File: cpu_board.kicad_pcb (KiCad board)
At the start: 2 copper layers, 19 parts, among them P1 USB_B, SW1 SW_PUSH, U1 MC6809, U2 MC6850, U3 NE555, U4 74HC04, Y1 4MHz

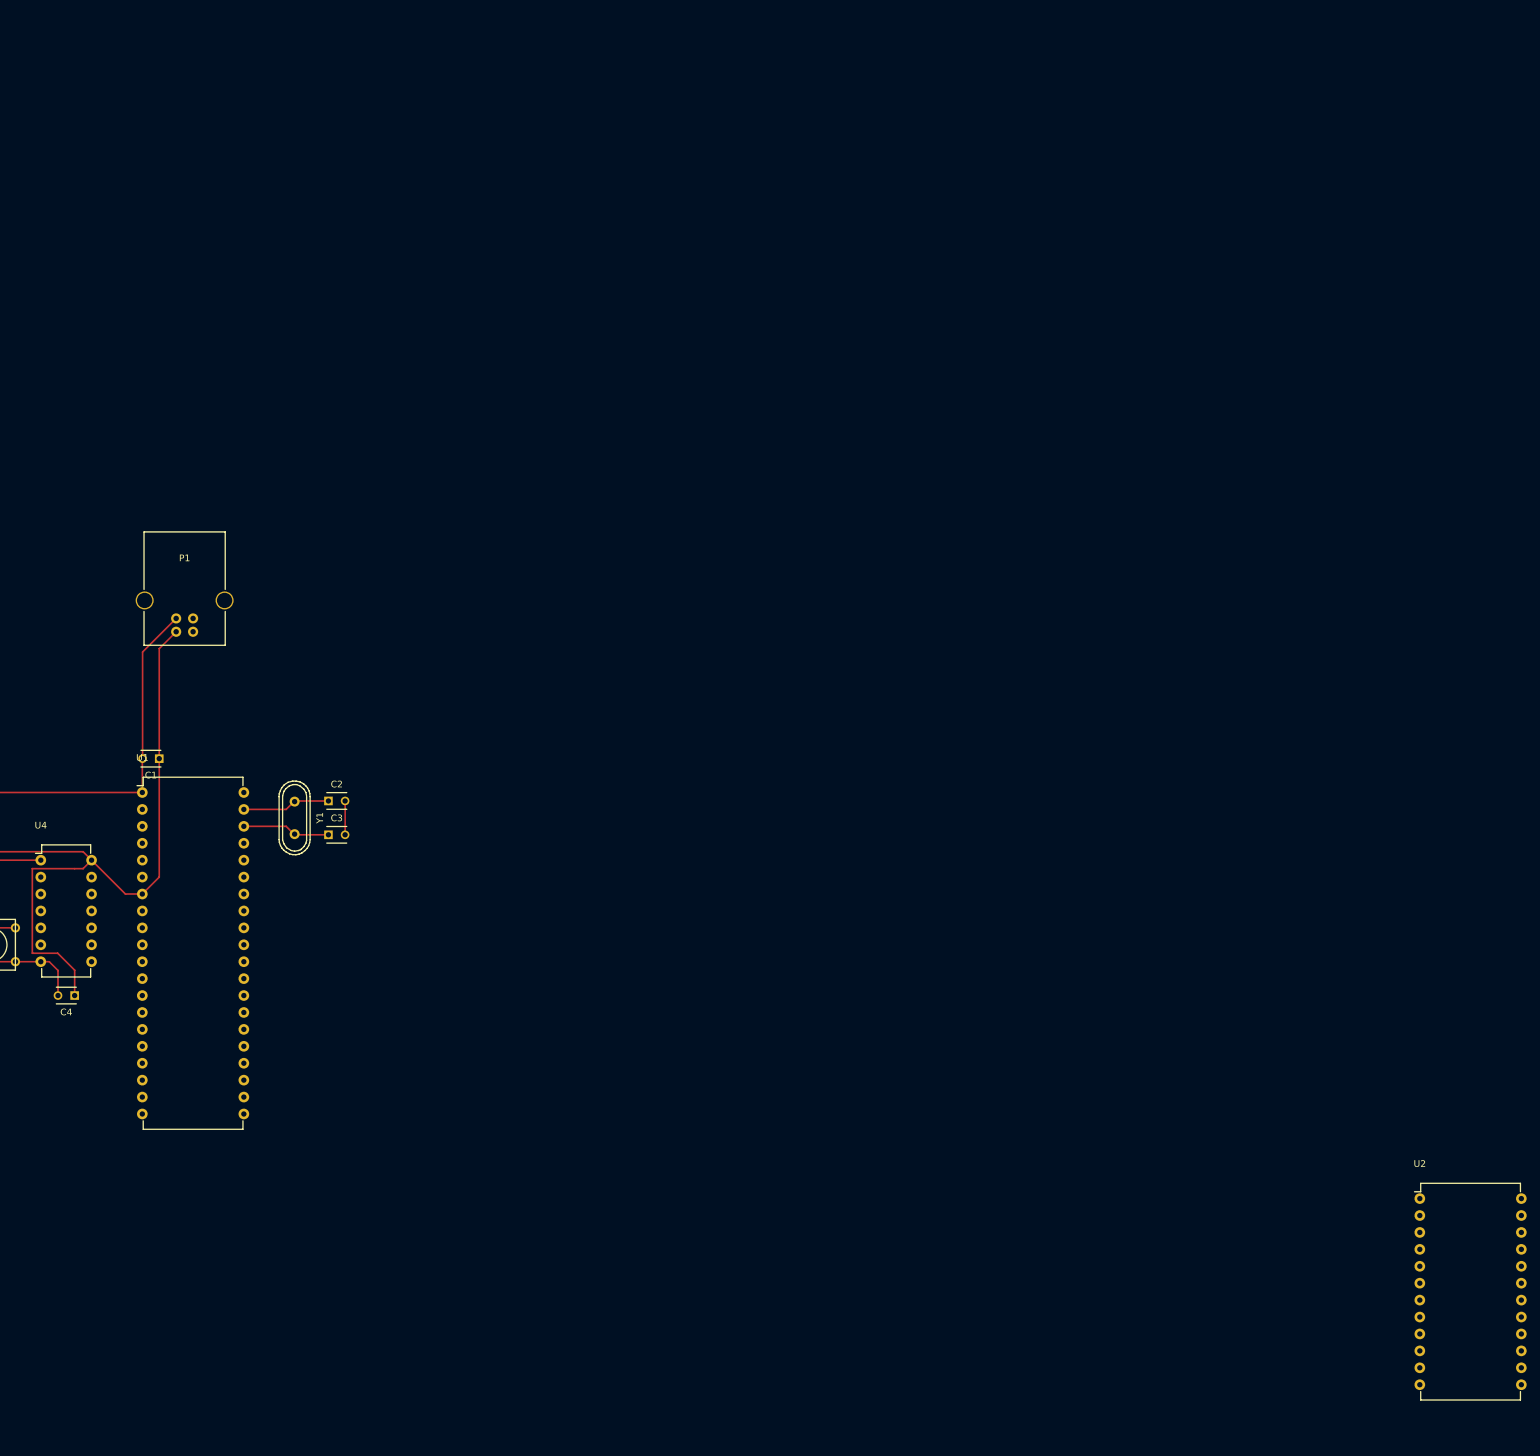
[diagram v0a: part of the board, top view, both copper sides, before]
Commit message: Added initial banking schematics
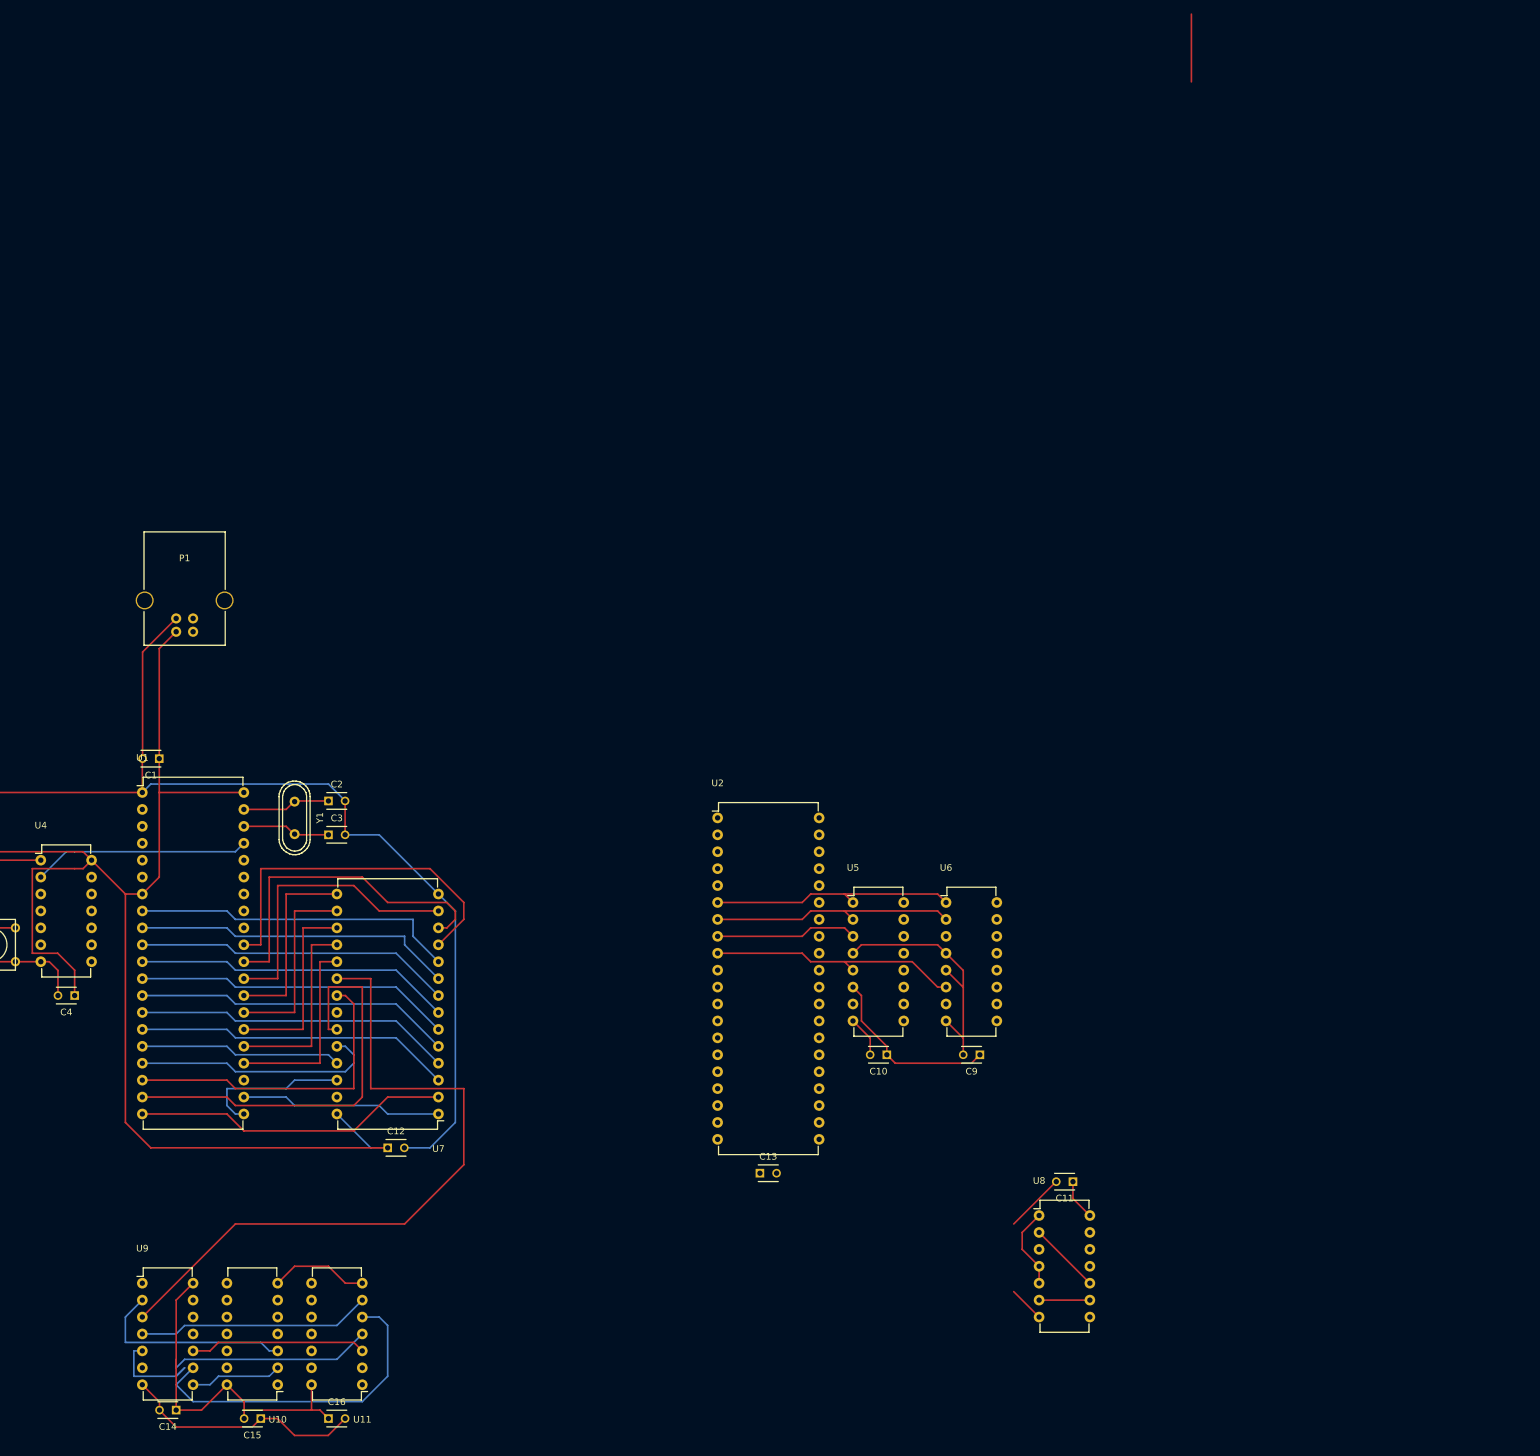
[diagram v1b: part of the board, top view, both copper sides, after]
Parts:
- added C10: 100nF, Capacitors_ThroughHole:C_Disc_D3_P2.5, F.Cu at (185.4, 118.1)
- added C11: 100nF, Capacitors_ThroughHole:C_Disc_D3_P2.5, F.Cu at (213.4, 137.2)
- added C12: 100nF, Capacitors_ThroughHole:C_Disc_D3_P2.5, F.Cu at (110.5, 132.1)
- added C13: 100nF, Capacitors_ThroughHole:C_Disc_D3_P2.5, F.Cu at (166.4, 135.9)
- added C14: 100nF, Capacitors_ThroughHole:C_Disc_D3_P2.5, F.Cu at (78.7, 171.4)
- added C15: 100nF, Capacitors_ThroughHole:C_Disc_D3_P2.5, F.Cu at (91.4, 172.7)
- added C16: 100nF, Capacitors_ThroughHole:C_Disc_D3_P2.5, F.Cu at (101.6, 172.7)
- added C9: 100nF, Capacitors_ThroughHole:C_Disc_D3_P2.5, F.Cu at (199.4, 118.1)
- added U10: 7400, Housings_DIP:DIP-14_W7.62mm, F.Cu at (94.0, 167.6)
- added U11: 74LS04, Housings_DIP:DIP-14_W7.62mm, F.Cu at (106.7, 167.6)
- added U5: 74LS138, Housings_DIP:DIP-16_W7.62mm, F.Cu at (180.3, 95.2)
- added U6: 74LS138, Housings_DIP:DIP-16_W7.62mm, F.Cu at (194.3, 95.2)
- added U7: HM62256BLP-7, Housings_DIP:DIP-28_W15.24mm, F.Cu at (118.1, 127.0)
- added U8: 7400, Housings_DIP:DIP-14_W7.62mm, F.Cu at (208.3, 142.2)
- added U9: 74LS08, Housings_DIP:DIP-14_W7.62mm, F.Cu at (73.7, 152.4)
- C2, C3: value 24pF -> 24/20/18/15pF
- U2: value MC6850 -> 6821; footprint Housings_DIP:DIP-24_W15.24mm -> Housings_DIP:DIP-40_W15.24mm
- Y1: value 4MHz -> 4/6/8/12MHz
- moved U2 119.9 mm to (160.0, 82.5)
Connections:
- U1 pad 10: Net-(U1-Pad10) -> A2
- U1 pad 11: Net-(U1-Pad11) -> A3
- U1 pad 12: Net-(U1-Pad12) -> A4
- U1 pad 13: Net-(U1-Pad13) -> A5
- U1 pad 14: Net-(U1-Pad14) -> A6
- U1 pad 15: Net-(U1-Pad15) -> A7
- U1 pad 16: Net-(U1-Pad16) -> A8
- U1 pad 17: Net-(U1-Pad17) -> A9
- U1 pad 18: Net-(U1-Pad18) -> A10
- U1 pad 19: Net-(U1-Pad19) -> A11
- U1 pad 20: Net-(U1-Pad20) -> A12
- U1 pad 21: Net-(U1-Pad21) -> A13
- U1 pad 22: Net-(U1-Pad22) -> A14
- U1 pad 23: Net-(U1-Pad23) -> A15
- U1 pad 24: Net-(U1-Pad24) -> D7
- U1 pad 25: Net-(U1-Pad25) -> D6
- U1 pad 26: Net-(U1-Pad26) -> D5
- U1 pad 27: Net-(U1-Pad27) -> D4
- U1 pad 28: Net-(U1-Pad28) -> D3
- U1 pad 29: Net-(U1-Pad29) -> D2
- U1 pad 30: Net-(U1-Pad30) -> D1
- U1 pad 31: Net-(U1-Pad31) -> D0
- U1 pad 32: Net-(U1-Pad32) -> /memory/R/~W~
- U1 pad 34: Net-(U1-Pad34) -> /memory/E
- U1 pad 40: Net-(U1-Pad40) -> +5V
- U1 pad 8: Net-(U1-Pad8) -> A0
- U1 pad 9: Net-(U1-Pad9) -> A1
- U2 pad 1: Net-(U2-Pad1) -> GND
- U2 pad 10: Net-(U1-Pad22) -> Net-(U2-Pad10)
- U2 pad 11: Net-(U1-Pad8) -> Net-(U2-Pad11)
- U2 pad 13: Net-(U1-Pad32) -> Net-(U2-Pad13)
- U2 pad 14: Net-(U1-Pad34) -> Net-(U2-Pad14)
- U2 pad 2: Net-(U2-Pad2) -> /memory/fixed_memory/bank
- U2 pad 20: Net-(U2-Pad20) -> +5V
- U2 pad 21: Net-(U2-Pad21) -> /memory/R/~W~
- U2 pad 3: Net-(U1-Pad34) -> Net-(U2-Pad3)
- U2 pad 4: Net-(U1-Pad34) -> Net-(U2-Pad4)
- U2 pad 8: Net-(U1-Pad23) -> Net-(U2-Pad8)
- U2 pad 9: Net-(U1-Pad21) -> Net-(U2-Pad9)
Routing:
- net GND: track 137.7 -> 342.5 mm
- net +5V: track 148.2 -> 331.7 mm
- net Net-(U7-Pad20): track 0.00 -> 104.7 mm
- net A14: track 0.00 -> 80.2 mm
- net A11: track 0.00 -> 63.3 mm
- net D0: track 0.00 -> 54.5 mm
- net D1: track 0.00 -> 50.9 mm
- net A0: track 0.00 -> 49.1 mm
- net Net-(U11-Pad4): track 0.00 -> 48.9 mm
- net A1: track 0.00 -> 48.4 mm
- net A10: track 0.00 -> 48.0 mm
- net A7: track 0.00 -> 47.6 mm
- net A5: track 0.00 -> 47.6 mm
- net A3: track 0.00 -> 47.6 mm
- net A2: track 0.00 -> 47.6 mm
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
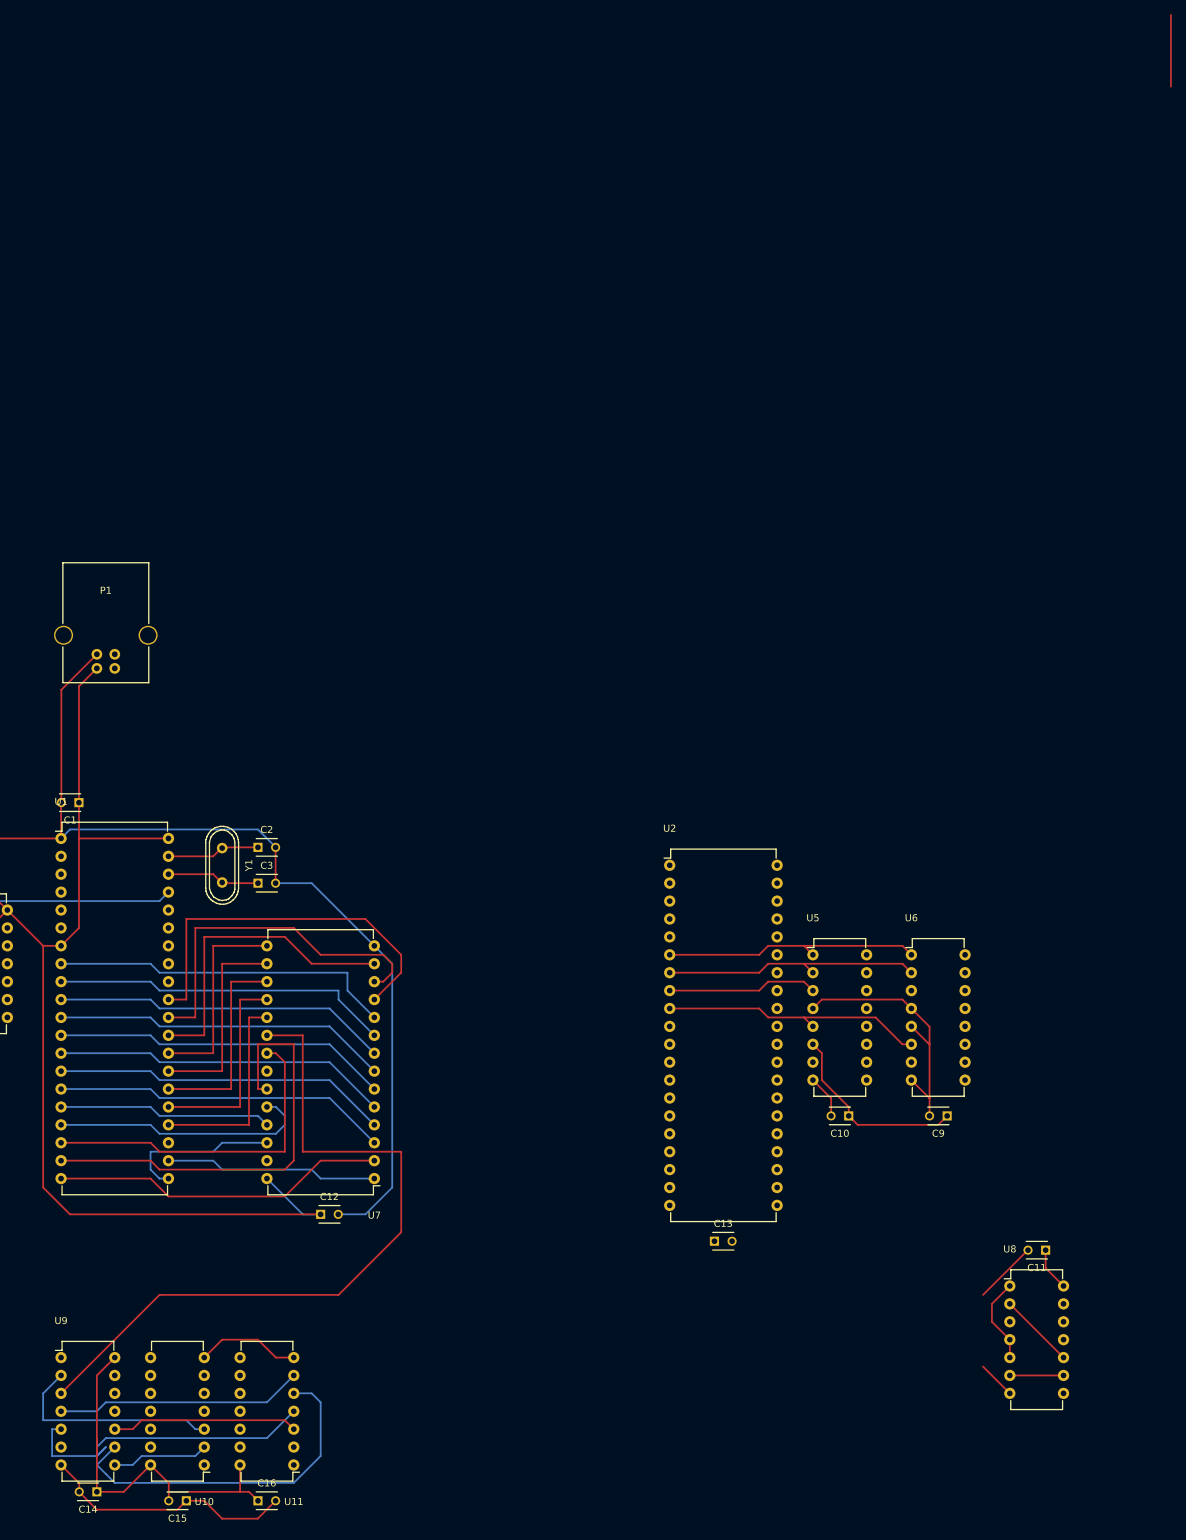
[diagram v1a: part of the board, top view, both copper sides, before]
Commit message: Added more tracks to memory selection
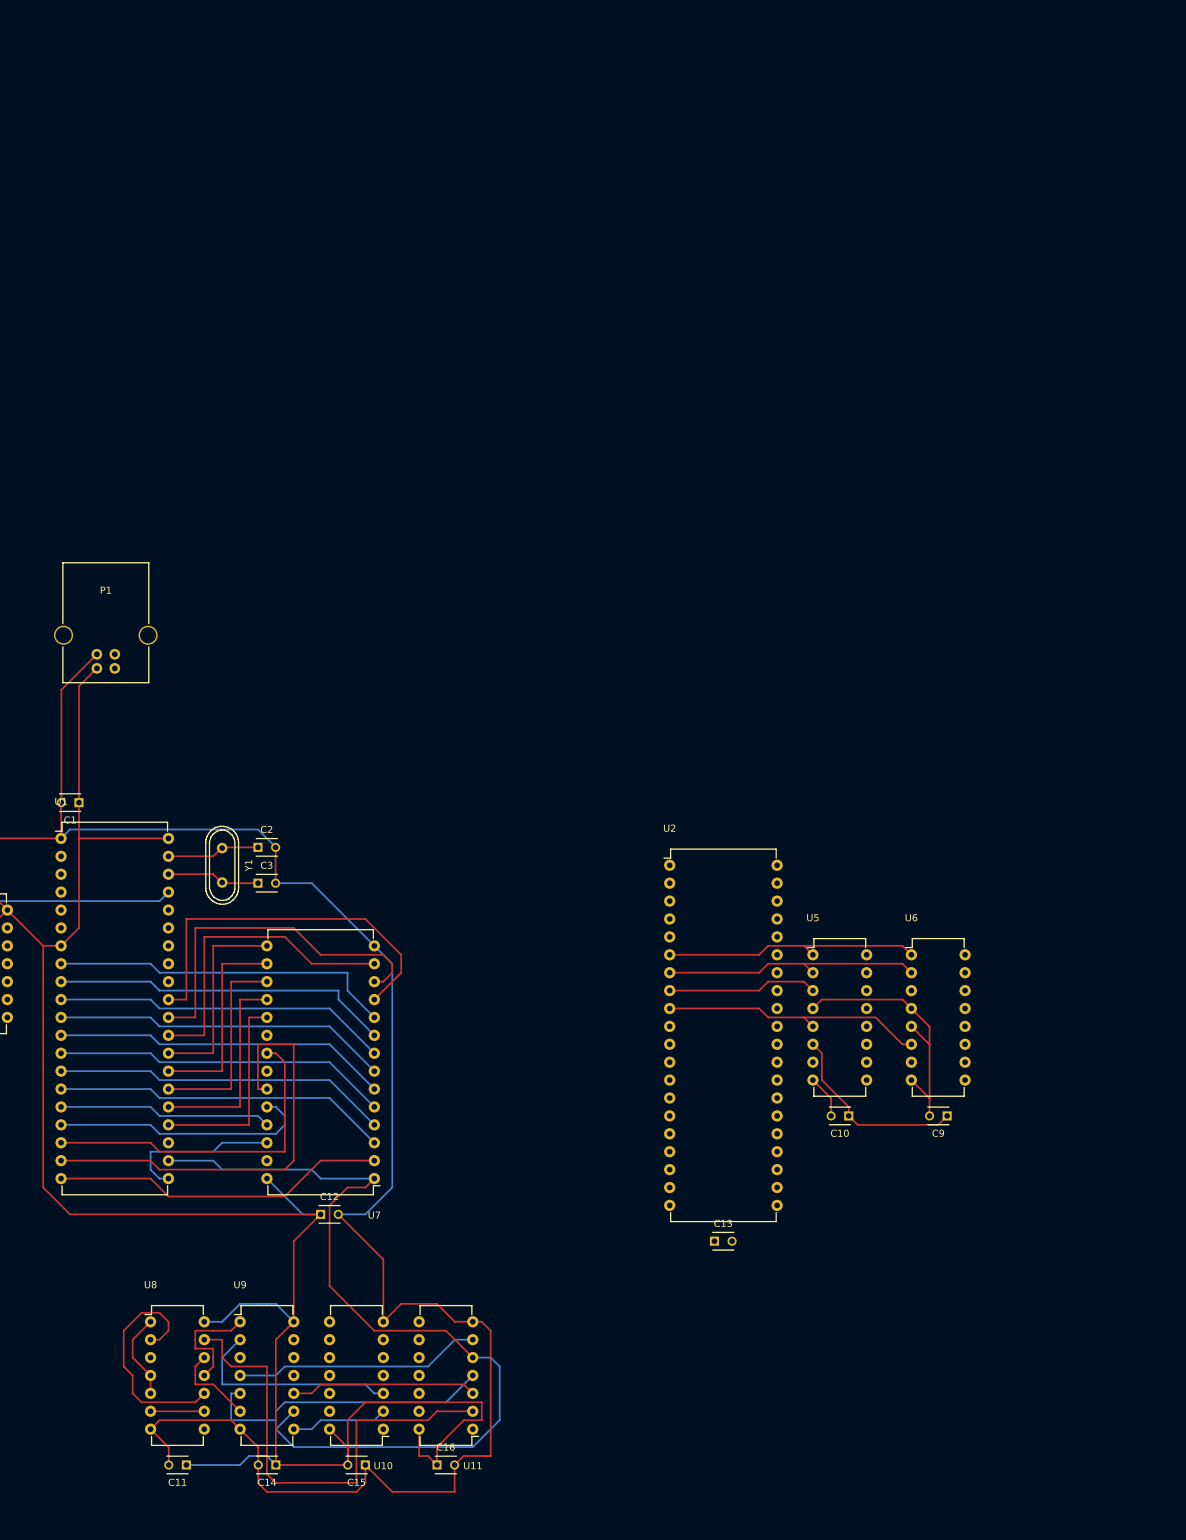
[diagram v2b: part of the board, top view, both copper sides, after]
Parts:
- moved C11 125.7 mm to (91.4, 167.6)
- moved U8 122.0 mm to (86.4, 147.3)
- moved C15 25.9 mm to (116.8, 167.6)
- moved C16 25.9 mm to (127.0, 167.6)
- moved U9 25.9 mm to (99.1, 147.3)
- moved U11 25.9 mm to (132.1, 162.6)
- moved U10 25.9 mm to (119.4, 162.6)
- moved C14 25.7 mm to (104.1, 167.6)
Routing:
- net Net-(U7-Pad20): track 104.7 -> 0.00 mm
- net +5V: track 331.7 -> 402.6 mm
- net Net-(U11-Pad2): track 0.00 -> 66.3 mm
- net GND: track 342.5 -> 402.9 mm
- net A14: track 80.2 -> 124.1 mm
- net /memory/rw_control/E: track 10.8 -> 32.9 mm
- net Net-(U8-Pad11): track 0.00 -> 16.3 mm
- net Net-(U8-Pad12): track 0.00 -> 12.3 mm
- net (no net): track 10.2 -> 0.00 mm
- net Net-(U11-Pad4): track 48.9 -> 42.7 mm

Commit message: Replaced descrete logic chips with decoder
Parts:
- removed C15, C16: 100nF, Capacitors_ThroughHole:C_Disc_D3_P2.5
- removed U10: 7400, Housings_DIP:DIP-14_W7.62mm
- removed U11: 74LS04, Housings_DIP:DIP-14_W7.62mm
- added P2: CONN_02X08, Pin_Headers:Pin_Header_Straight_2x08, F.Cu at (241.3, 111.8)
- added P3: CONN_02X12, Pin_Headers:Pin_Header_Straight_2x12, F.Cu at (241.3, 76.2)
- U9: value 74LS08 -> 74LS139
- moved C11 49.9 mm to (41.9, 161.3)
- moved U8 49.9 mm to (36.8, 141.0)
- moved C14 27.7 mm to (96.5, 141.0), turned to 90 degrees
- moved U9 13.7 mm to (91.4, 135.9), turned to 270 degrees
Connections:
- U1 pad 37: /reset_circuit/reset -> /memory/reset
- U4 pad 2: /reset_circuit/reset -> /memory/reset
- U8 pad 11: Net-(U8-Pad11) -> (no net)
- U8 pad 12: Net-(U8-Pad12) -> (no net)
- U8 pad 13: Net-(U11-Pad2) -> (no net)
- U9 pad 1: Net-(U8-Pad11) -> GND
- U9 pad 10: A15 -> (no net)
- U9 pad 14: +5V -> (no net)
- U9 pad 2: Net-(U10-Pad3) -> A14
- U9 pad 3: Net-(U7-Pad20) -> A15
- U9 pad 4: Net-(U11-Pad6) -> /memory/fixed_ram_enable
- U9 pad 5: Net-(U11-Pad4) -> /memory/banked_ram_enable
- U9 pad 6: Net-(U8-Pad12) -> /memory/io_enable_pin
- U9 pad 7: GND -> /memory/rom_enable
- U9 pad 8: Net-(U10-Pad2) -> GND
- U9 pad 9: A14 -> (no net)
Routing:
- net +5V: track 402.6 -> 273.2 mm
- net GND: track 402.9 -> 322.0 mm
- net A14: track 124.1 -> 43.8 mm
- net Net-(U11-Pad2): track 66.3 -> 0.00 mm
- net Net-(U11-Pad4): track 42.7 -> 0.00 mm
- net Net-(U11-Pad6): track 35.1 -> 0.00 mm
- net /memory/rw_control/E: track 32.9 -> 0.00 mm
- net /reset_circuit/reset: track 32.6 -> 0.00 mm
- net /memory/reset: track 0.00 -> 32.6 mm
- net Net-(U10-Pad3): track 30.8 -> 0.00 mm
- net Net-(U8-Pad11): track 16.3 -> 0.00 mm
- net Net-(U10-Pad2): track 13.8 -> 0.00 mm
- net Net-(U8-Pad12): track 12.3 -> 0.00 mm
- net /memory/rw_control/R/~W~: track 12.3 -> 2.54 mm
- net A15: track 26.5 -> 17.6 mm
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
